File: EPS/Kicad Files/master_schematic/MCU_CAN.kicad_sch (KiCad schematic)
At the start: 8 parts, among them U1 PIC18F27Q84-E/SP, U2 ATA6560-GAQW-VAO

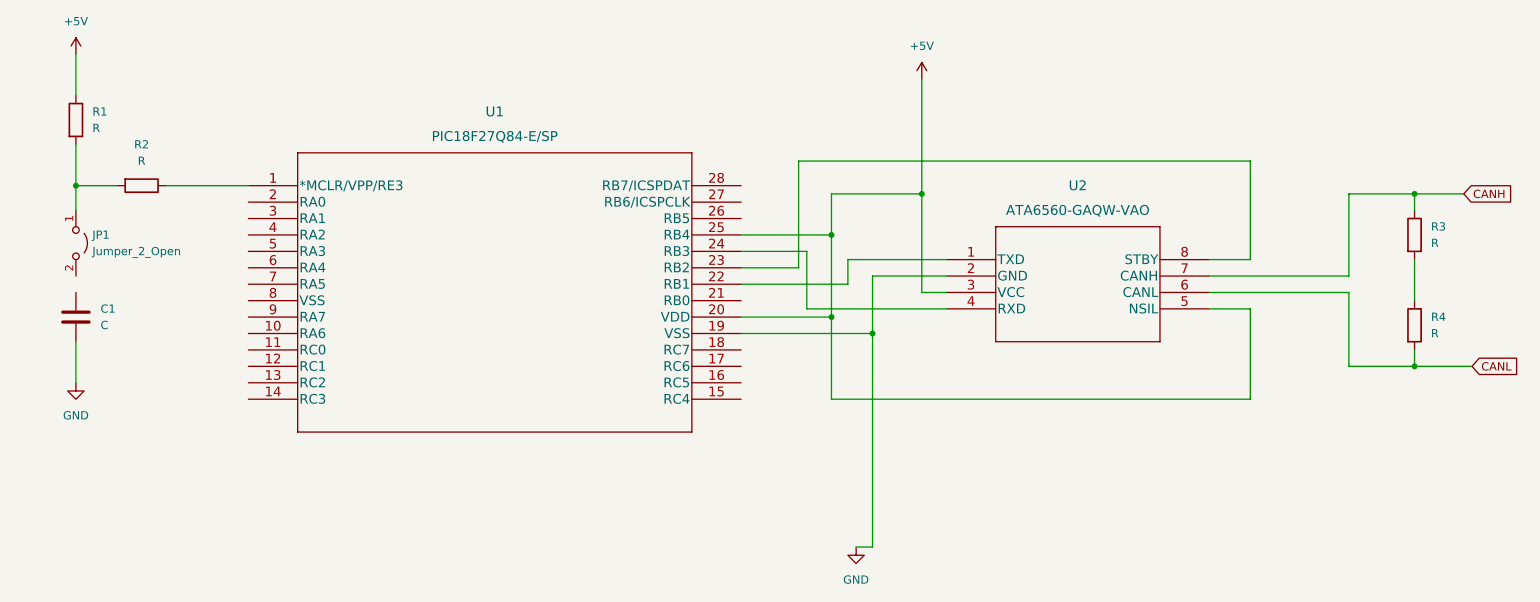
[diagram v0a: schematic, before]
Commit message: master schematic update
added hierarchal pins to MCU_CAN, and attached it with the rest of the circuit
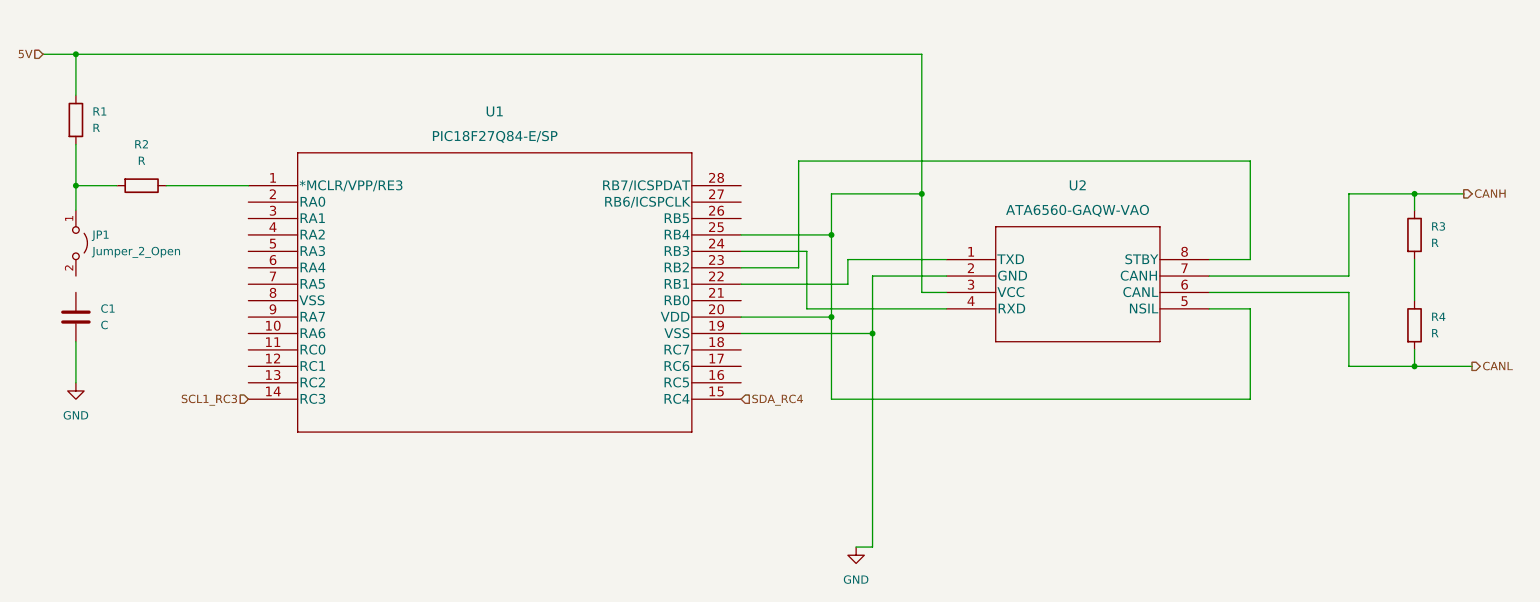
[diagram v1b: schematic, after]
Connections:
- net SCL1_RC3: now reaches U1.14 (RC3)
- net SDA_RC4: now reaches U1.15 (RC4)
- net +5V renamed 5V
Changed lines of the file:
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@@
   (junction (at 172.72 76.2) (diameter 0) (color 0 0 0 0)
   )
+  (junction (at 49.53 33.02) (diameter 0) (color 0 0 0 0)
+  )
   (junction (at 180.34 54.61) (diameter 0) (color 0 0 0 0)
   )
@@
     (stroke (width 0) (type default) (color 0 0 0 0))
   )
-  (wire (pts (xy 180.34 36.83) (xy 180.34 54.61))
+  (wire (pts (xy 49.53 33.02) (xy 180.34 33.02))
+    (stroke (width 0) (type default) (color 0 0 0 0))
+  )
+  (wire (pts (xy 180.34 33.02) (xy 180.34 54.61))
     (stroke (width 0) (type default) (color 0 0 0 0))
   )
@@
     (stroke (width 0) (type default) (color 0 0 0 0))
   )
+  (wire (pts (xy 44.45 33.02) (xy 49.53 33.02))
+    (stroke (width 0) (type default) (color 0 0 0 0))
+  )
   (wire (pts (xy 256.54 78.74) (xy 256.54 81.28))
     (stroke (width 0) (type default) (color 0 0 0 0))
@@
     (stroke (width 0) (type default) (color 0 0 0 0))
   )
-  (global_label "CANH" (shape input) (at 264.16 54.61 0) (fields_autoplaced)
+  (hierarchical_label "SDA_RC4" (shape input) (at 152.4 86.36 0)
     (effects (font (size 1.27 1.27)) (justify left))
-    (property "Intersheet References" "${INTERSHEET_REFS}" (id 0) (at 271.5926 54.5306 0)
-      (effects (font (size 1.27 1.27)) (justify left) hide)
-    )
-  )
-  (global_label "CANL" (shape input) (at 265.43 81.28 0) (fields_autoplaced)
+  )
+  (hierarchical_label "SCL1_RC3" (shape input) (at 76.2 86.36 180)
+    (effects (font (size 1.27 1.27)) (justify right))
+  )
+  (hierarchical_label "CANL" (shape output) (at 265.43 81.28 0)
     (effects (font (size 1.27 1.27)) (justify left))
-    (property "Intersheet References" "${INTERSHEET_REFS}" (id 0) (at 272.5602 81.2006 0)
-      (effects (font (size 1.27 1.27)) (justify left) hide)
-    )
+  )
+  (hierarchical_label "CANH" (shape output) (at 264.16 54.61 0)
+    (effects (font (size 1.27 1.27)) (justify left))
+  )
+  (hierarchical_label "5V" (shape input) (at 44.45 33.02 180)
+    (effects (font (size 1.27 1.27)) (justify right))
   )
   (symbol (lib_id "Device:R") (at 256.54 74.93 0) (unit 1)
@@
     (pin "7")
     (pin "8")
-  )
-  (symbol (lib_id "power:+5V") (at 49.53 33.02 0) (unit 1)
-    (in_bom yes) (on_board yes)
-    (property "Reference" "#PWR0101" (id 0) (at 49.53 36.83 0)
-      (effects (font (size 1.27 1.27)) hide)
-    )
-    (property "Value" "+5V" (id 1) (at 49.53 27.94 0))
-    (property "Footprint" "" (id 2) (at 49.53 33.02 0)
-      (effects (font (size 1.27 1.27)) hide)
-    )
-    (property "Datasheet" "" (id 3) (at 49.53 33.02 0)
-      (effects (font (size 1.27 1.27)) hide)
-    )
-    (pin "1")
   )
   (symbol (lib_id "power:GND") (at 170.18 109.22 0) (unit 1)
@@
     (pin "9")
   )
-  (symbol (lib_id "power:+5V") (at 180.34 36.83 0) (unit 1)
-    (in_bom yes) (on_board yes)
-    (property "Reference" "#PWR0104" (id 0) (at 180.34 40.64 0)
-      (effects (font (size 1.27 1.27)) hide)
-    )
-    (property "Value" "+5V" (id 1) (at 180.34 31.75 0))
-    (property "Footprint" "" (id 2) (at 180.34 36.83 0)
-      (effects (font (size 1.27 1.27)) hide)
-    )
-    (property "Datasheet" "" (id 3) (at 180.34 36.83 0)
-      (effects (font (size 1.27 1.27)) hide)
-    )
-    (pin "1")
-  )
   (symbol (lib_id "power:GND") (at 49.53 83.82 0) (unit 1)
